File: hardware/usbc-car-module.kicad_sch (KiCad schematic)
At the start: 0 parts

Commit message: making hardware progress
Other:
- sheet FRONT USB-C POWER renamed USB-C_POWER
- added sheet ADC (ADC.kicad_sch)
- added sheet ESP-12F (ESP-12F.kicad_sch)
- note added: "ADJ BACK USB-PD BUCK-CONVERTER"
- note added: "USB VOLTAGE CHECK ADC ADS7128IRTER"
- note removed: "LM5157x"
- note removed: "TLE9251VSJXUMA1"
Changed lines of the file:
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@@
     (stroke (width 0) (type default))
   )
-  (polyline (pts (xy 109.22 107.95) (xy 140.97 107.95))
+  (polyline (pts (xy 109.22 107.95) (xy 153.67 107.95))
     (stroke (width 0) (type default))
   )
@@
     (stroke (width 0) (type default))
   )
-  (polyline (pts (xy 144.78 111.76) (xy 144.78 144.78))
-    (stroke (width 0) (type default))
-  )
   (polyline (pts (xy 76.2 54.61) (xy 87.63 54.61))
     (stroke (width 0) (type default))
@@
   )
   (rectangle (start 134.62 44.45) (end 148.59 50.8)
-    (stroke (width 0) (type default))
-    (fill (type color) (color 134 255 169 1))
-  )
-  (rectangle (start 50.8 49.53) (end 63.5 62.23)
     (stroke (width 0) (type default))
     (fill (type color) (color 134 255 169 1))
@@
     (effects (font (size 1.27 1.27)) (justify left top))
   )
-  (text_box "ADJ BACK USB-PD\nBUCK-CONVERTER"
-    (at 82.55 119.38 0) (size 25.4 6.35)
+  (text_box "1.2V LDO"
+    (at 93.98 85.09 0) (size 11.43 3.81)
     (stroke (width 0) (type default))
     (fill (type none))
     (effects (font (size 1.27 1.27)) (justify left top))
   )
-  (text_box "1.2V LDO"
-    (at 93.98 85.09 0) (size 11.43 3.81)
+  (text_box "CAR 12V-IN"
+    (at 21.59 102.87 0) (size 13.97 6.35)
     (stroke (width 0) (type default))
     (fill (type none))
     (effects (font (size 1.27 1.27)) (justify left top))
   )
-  (text_box "CAR 12V-IN"
-    (at 21.59 102.87 0) (size 13.97 6.35)
-    (stroke (width 0) (type default))
-    (fill (type none))
-    (effects (font (size 1.27 1.27)) (justify left top))
-  )
-  (text_box "USB VOLTAGE CHECK ADC\nADS7128IRTER"
-    (at 127 146.05 0) (size 22.86 12.7)
-    (stroke (width 0) (type default))
-    (fill (type none))
-    (effects (font (size 1.27 1.27)) (justify left top))
-  )
-  (text_box "CURRENT\nSHUNT"
-    (at 142.24 105.41 0) (size 10.16 5.08)
-    (stroke (width 0) (type default))
-    (fill (type none))
-    (effects (font (size 1.27 1.27)) (justify left top))
-  )
   (text "BACK (UFP)\nUSB-C" (at 135.89 49.53 0)
     (effects (font (size 1.27 1.27)) (justify left bottom))
@@
   )
   (text "CONTROLL + ENABEL SIGNALS" (at 59.69 78.74 0)
+    (effects (font (size 1.27 1.27)) (justify left bottom))
+  )
+  (text "USB VOLTAGE CHECK \nADC\nADS7128IRTER" (at 128.27 153.67 0)
     (effects (font (size 1.27 1.27)) (justify left bottom))
   )
@@
     (effects (font (size 1.27 1.27)) (justify left bottom))
   )
+  (text "ADJ BACK USB-PD\nBUCK-CONVERTER" (at 83.82 124.46 0)
+    (effects (font (size 1.27 1.27)) (justify left bottom))
+  )
   (text "CLOCK SYNC??" (at 44.45 120.65 0)
     (effects (font (size 1.27 1.27)) (justify left bottom))
@@
     (effects (font (size 1.27 1.27)) (justify left bottom))
   )
-  (text "LM5157x" (at 90.17 129.54 0)
-    (effects (font (size 1.27 1.27)) (justify left bottom))
-  )
   (text "21V BOOST-CONVERTER" (at 44.45 105.41 0)
     (effects (font (size 1.27 1.27)) (justify left bottom))
@@
     (effects (font (size 1.27 1.27)) (justify left bottom))
   )
-  (text "TLE9251VSJXUMA1" (at 27.94 73.66 0)
-    (effects (font (size 1.27 1.27)) (justify left bottom))
-  )
   (text "ESP-12F" (at 52.07 55.88 0)
     (effects (font (size 1.27 1.27)) (justify left bottom))
@@
     (effects (font (size 1.27 1.27)) (justify left bottom))
   )
-  (sheet (at 82.55 111.76) (size 25.4 6.35) (fields_autoplaced)
-    (stroke (width 0.1524) (type solid))
-    (fill (color 0 0 0 0.0000))
-    (property "Sheetname" "FRONT USB-C POWER" (at 82.55 111.0484 0)
-      (effects (font (size 1.27 1.27)) (justify left bottom))
-    )
-    (property "Sheetfile" "FRONT USB-C POWER.kicad_sch" (at 82.55 118.6946 0)
+  (sheet (at 50.8 49.53) (size 12.7 12.7) (fields_autoplaced)
+    (stroke (width 0.1524) (type solid))
+    (fill (color 0 0 0 0.0000))
+    (property "Sheetname" "ESP-12F" (at 50.8 48.8184 0)
+      (effects (font (size 1.27 1.27)) (justify left bottom))
+    )
+    (property "Sheetfile" "ESP-12F.kicad_sch" (at 50.8 62.8146 0)
+      (effects (font (size 1.27 1.27)) (justify left top))
+    )
+    (instances
+      (project "usbc-car-module"
+        (path "/fae025e9-99c5-40c1-af6f-99dc1edbfa43" (page "6"))
+      )
+    )
+  )
+  (sheet (at 82.55 111.76) (size 25.4 13.97) (fields_autoplaced)
+    (stroke (width 0.1524) (type solid))
+    (fill (color 0 0 0 0.0000))
+    (property "Sheetname" "USB-C_POWER" (at 82.55 111.0484 0)
+      (effects (font (size 1.27 1.27)) (justify left bottom))
+    )
+    (property "Sheetfile" "FRONT USB-C POWER.kicad_sch" (at 82.55 126.3146 0)
       (effects (font (size 1.27 1.27)) (justify left top))
     )
@@
       )
     )
+  )
+  (sheet (at 127 146.05) (size 22.86 13.97) (fields_autoplaced)
+    (stroke (width 0.1524) (type solid))
+    (fill (color 0 0 0 0.0000))
+    (property "Sheetname" "ADC" (at 127 145.3384 0)
+      (effects (font (size 1.27 1.27)) (justify left bottom))
+    )
+    (property "Sheetfile" "ADC.kicad_sch" (at 127 160.6046 0)
+      (effects (font (size 1.27 1.27)) (justify left top))
+    )
+    (instances
+      (project "usbc-car-module"
+        (path "/fae025e9-99c5-40c1-af6f-99dc1edbfa43" (page "7"))
+      )
+    )

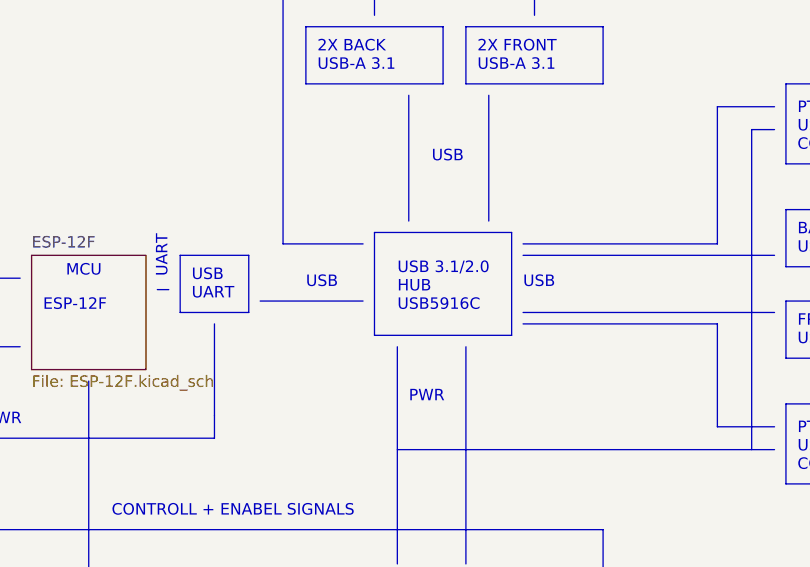
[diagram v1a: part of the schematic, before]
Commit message: working on usb side implimentaion
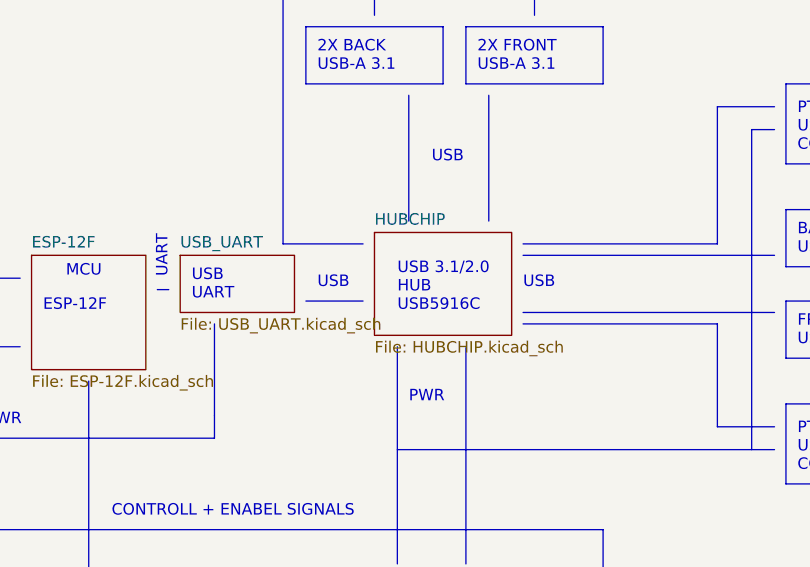
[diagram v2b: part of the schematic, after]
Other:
- added sheet HUBCHIP (HUBCHIP.kicad_sch)
- added sheet USB_UART (USB_UART.kicad_sch)
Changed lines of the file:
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@@
     (stroke (width 0) (type default))
   )
-  (polyline (pts (xy 76.2 54.61) (xy 87.63 54.61))
+  (polyline (pts (xy 81.28 54.61) (xy 87.63 54.61))
     (stroke (width 0) (type default))
   )
@@
     (stroke (width 0) (type default))
   )
-  (rectangle (start 88.9 46.99) (end 104.14 58.42)
-    (stroke (width 0) (type default))
-    (fill (type color) (color 134 255 169 1))
-  )
   (rectangle (start 134.62 54.61) (end 148.59 60.96)
     (stroke (width 0) (type default))
@@
   )
   (rectangle (start 24.13 48.26) (end 43.18 54.61)
-    (stroke (width 0) (type default))
-    (fill (type color) (color 134 255 169 1))
-  )
-  (rectangle (start 67.31 49.53) (end 74.93 55.88)
     (stroke (width 0) (type default))
     (fill (type color) (color 134 255 169 1))
@@
     (effects (font (size 1.27 1.27)) (justify left bottom))
   )
-  (text "USB" (at 81.28 53.34 0)
+  (text "USB" (at 82.55 53.34 0)
     (effects (font (size 1.27 1.27)) (justify left bottom))
   )
@@
   (text "USB" (at 95.25 39.37 0)
     (effects (font (size 1.27 1.27)) (justify left bottom))
+  )
+  (sheet (at 67.31 49.53) (size 12.7 6.35) (fields_autoplaced)
+    (stroke (width 0.1524) (type solid))
+    (fill (color 0 0 0 0.0000))
+    (property "Sheetname" "USB_UART" (at 67.31 48.8184 0)
+      (effects (font (size 1.27 1.27)) (justify left bottom))
+    )
+    (property "Sheetfile" "USB_UART.kicad_sch" (at 67.31 56.4646 0)
+      (effects (font (size 1.27 1.27)) (justify left top))
+    )
+    (property "Field2" "" (at 67.31 49.53 0)
+      (effects (font (size 1.27 1.27)) hide)
+    )
+    (instances
+      (project "usbc-car-module"
+        (path "/fae025e9-99c5-40c1-af6f-99dc1edbfa43" (page "9"))
+      )
+    )
   )
   (sheet (at 50.8 49.53) (size 12.7 12.7) (fields_autoplaced)
@@
       )
     )
+  )
+  (sheet (at 88.9 46.99) (size 15.24 11.43) (fields_autoplaced)
+    (stroke (width 0.1524) (type solid))
+    (fill (color 0 0 0 0.0000))
+    (property "Sheetname" "HUBCHIP" (at 88.9 46.2784 0)
+      (effects (font (size 1.27 1.27)) (justify left bottom))
+    )
+    (property "Sheetfile" "HUBCHIP.kicad_sch" (at 88.9 59.0046 0)
+      (effects (font (size 1.27 1.27)) (justify left top))
+    )
+    (instances
+      (project "usbc-car-module"
+        (path "/fae025e9-99c5-40c1-af6f-99dc1edbfa43" (page "8"))
+      )
+    )

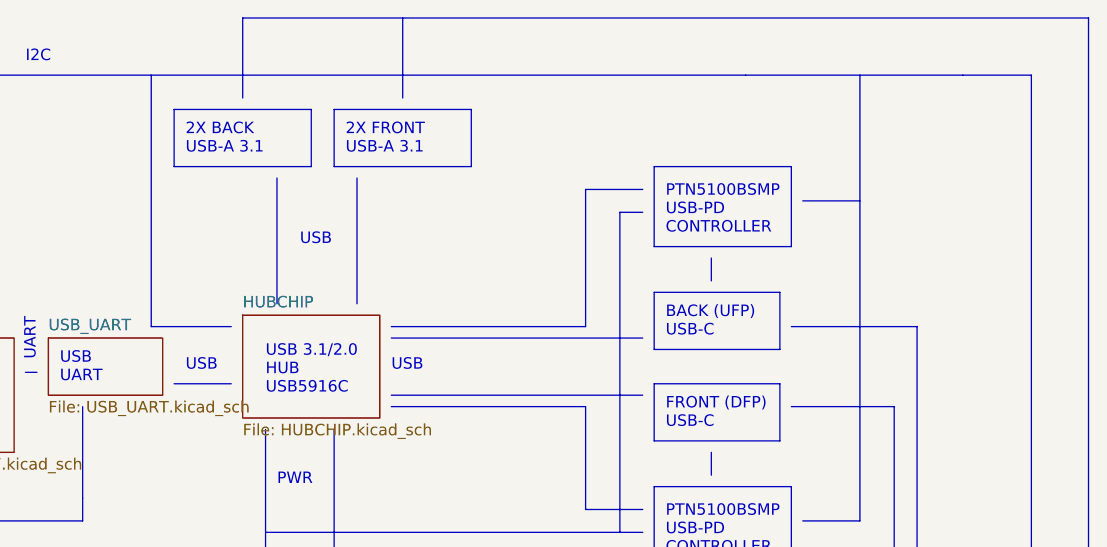
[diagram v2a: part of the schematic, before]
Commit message: working on hardware agin as well as implimentded auto adc init and read
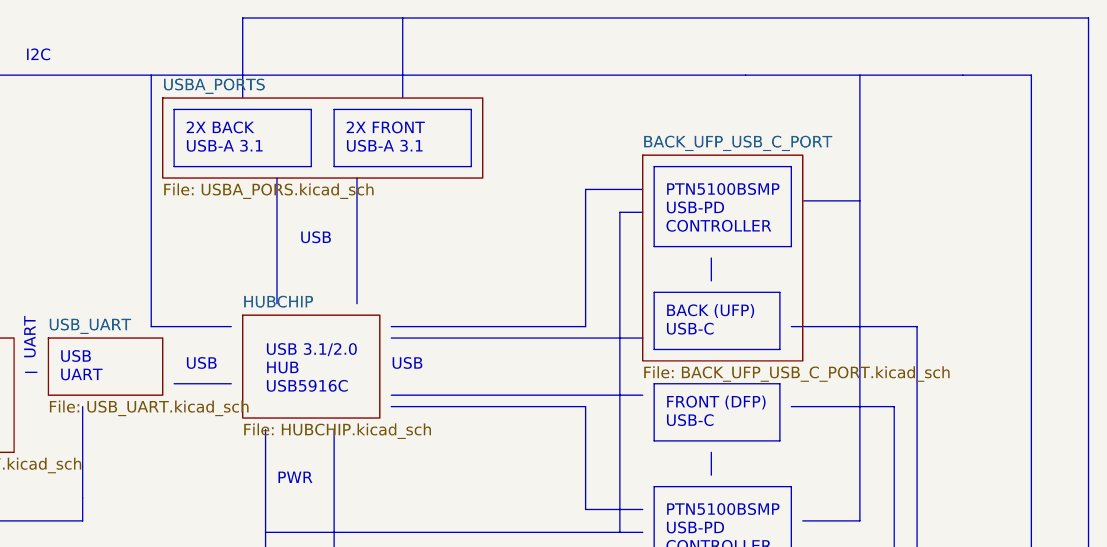
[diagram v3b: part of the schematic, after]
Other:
- added sheet BACK_UFP_USB_C_PORT (BACK_UFP_USB_C_PORT.kicad_sch)
- added sheet USBA_PORTS (USBA_PORS.kicad_sch)
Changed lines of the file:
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@@
+    )
+  )
+  (sheet (at 133.35 29.21) (size 17.78 22.86) (fields_autoplaced)
+    (stroke (width 0.1524) (type solid))
+    (fill (color 0 0 0 0.0000))
+    (property "Sheetname" "BACK_UFP_USB_C_PORT" (at 133.35 28.4984 0)
+      (effects (font (size 1.27 1.27)) (justify left bottom))
+    )
+    (property "Sheetfile" "BACK_UFP_USB_C_PORT.kicad_sch" (at 133.35 52.6546 0)
+      (effects (font (size 1.27 1.27)) (justify left top))
+    )
+    (instances
+      (project "usbc-car-module"
+        (path "/fae025e9-99c5-40c1-af6f-99dc1edbfa43" (page "11"))
+      )
     )
   )
@@
       )
     )
+  )
+  (sheet (at 80.01 22.86) (size 35.56 8.89) (fields_autoplaced)
+    (stroke (width 0.1524) (type solid))
+    (fill (color 0 0 0 0.0000))
+    (property "Sheetname" "USBA_PORTS" (at 80.01 22.1484 0)
+      (effects (font (size 1.27 1.27)) (justify left bottom))
+    )
+    (property "Sheetfile" "USBA_PORS.kicad_sch" (at 80.01 32.3346 0)
+      (effects (font (size 1.27 1.27)) (justify left top))
+    )
+    (instances
+      (project "usbc-car-module"
+        (path "/fae025e9-99c5-40c1-af6f-99dc1edbfa43" (page "10"))
+      )
+    )

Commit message: finnished rudimentry schimatics still needs alot of work
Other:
- added sheet CAR_12V_IN (CAR_12V_IN.kicad_sch)
- added sheet FRONT_DFP_USB_C_PORT (FRONT_DFP_USB_C_PORT.kicad_sch)
- added sheet FRONT_PANNEL_DISPLAY (FRONT_PANNEL_DISPLAY.kicad_sch)
- note added: "CAR 12V-IN"
- note added: "FRONT PANNEL POWER DISPLAY"
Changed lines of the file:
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@@
+    (stroke (width 0) (type default))
+  )
+  (polyline (pts (xy 39.37 31.75) (xy 46.99 31.75))
     (stroke (width 0) (type default))
   )
@@
     (stroke (width 0) (type default))
   )
+  (polyline (pts (xy 16.51 59.69) (xy 16.51 31.75))
+    (stroke (width 0) (type default))
+  )
   (polyline (pts (xy 72.39 157.48) (xy 125.73 157.48))
     (stroke (width 0) (type default))
@@
     (stroke (width 0) (type default))
   )
+  (polyline (pts (xy 16.51 31.75) (xy 19.05 31.75))
+    (stroke (width 0) (type default))
+  )
+  (polyline (pts (xy 26.67 59.69) (xy 16.51 59.69))
+    (stroke (width 0) (type default))
+  )
   (polyline (pts (xy 71.12 67.31) (xy 71.12 69.85))
     (stroke (width 0) (type default))
@@
     (stroke (width 0) (type default))
     (fill (type color) (color 134 255 169 1))
+  )
+  (rectangle (start 50.8 49.53) (end 63.5 62.23)
+    (stroke (width 0) (type default))
+    (fill (type none))
   )
   (rectangle (start 134.62 66.04) (end 149.86 74.93)
@@
     (effects (font (size 1.27 1.27)) (justify left top))
   )
-  (text_box "CAR 12V-IN"
-    (at 21.59 102.87 0) (size 13.97 6.35)
-    (stroke (width 0) (type default))
-    (fill (type none))
-    (effects (font (size 1.27 1.27)) (justify left top))
-  )
   (text "BACK (UFP)\nUSB-C" (at 135.89 49.53 0)
     (effects (font (size 1.27 1.27)) (justify left bottom))
@@
   )
   (text "IO-EXPANDER\nPI4IOE5V6416LEX" (at 25.4 53.34 0)
+    (effects (font (size 1.27 1.27)) (justify left bottom))
+  )
+  (text "CAR 12V-IN" (at 21.59 105.41 0)
     (effects (font (size 1.27 1.27)) (justify left bottom))
   )
@@
     (effects (font (size 1.27 1.27)) (justify left bottom))
   )
+  (text "FRONT PANNEL \nPOWER DISPLAY" (at 21.59 30.48 0)
+    (effects (font (size 1.27 1.27)) (justify left bottom))
+  )
   (text "ADJ BACK USB-PD\nBUCK-CONVERTER" (at 83.82 124.46 0)
     (effects (font (size 1.27 1.27)) (justify left bottom))
@@
     )
   )
-  (sheet (at 50.8 49.53) (size 12.7 12.7) (fields_autoplaced)
-    (stroke (width 0.1524) (type solid))
-    (fill (color 0 0 0 0.0000))
-    (property "Sheetname" "ESP-12F" (at 50.8 48.8184 0)
-      (effects (font (size 1.27 1.27)) (justify left bottom))
-    )
-    (property "Sheetfile" "ESP-12F.kicad_sch" (at 50.8 62.8146 0)
+  (sheet (at 21.59 46.99) (size 43.18 19.05) (fields_autoplaced)
+    (stroke (width 0.1524) (type solid))
+    (fill (color 0 0 0 0.0000))
+    (property "Sheetname" "ESP-12F" (at 21.59 46.2784 0)
+      (effects (font (size 1.27 1.27)) (justify left bottom))
+    )
+    (property "Sheetfile" "ESP-12F.kicad_sch" (at 21.59 66.6246 0)
       (effects (font (size 1.27 1.27)) (justify left top))
     )
@@
     )
   )
+  (sheet (at 20.32 102.87) (size 13.97 6.35) (fields_autoplaced)
+    (stroke (width 0.1524) (type solid))
+    (fill (color 0 0 0 0.0000))
+    (property "Sheetname" "CAR_12V_IN" (at 20.32 102.1584 0)
+      (effects (font (size 1.27 1.27)) (justify left bottom))
+    )
+    (property "Sheetfile" "CAR_12V_IN.kicad_sch" (at 20.32 109.8046 0)
+      (effects (font (size 1.27 1.27)) (justify left top))
+    )
+    (instances
+      (project "usbc-car-module"
+        (path "/fae025e9-99c5-40c1-af6f-99dc1edbfa43" (page "14"))
+      )
+    )
+  )
   (sheet (at 88.9 46.99) (size 15.24 11.43) (fields_autoplaced)
     (stroke (width 0.1524) (type solid))
@@
       )
     )
+  )
+  (sheet (at 133.35 53.34) (size 17.78 22.86) (fields_autoplaced)
+    (stroke (width 0.1524) (type solid))
+    (fill (color 0 0 0 0.0000))
+    (property "Sheetname" "FRONT_DFP_USB_C_PORT" (at 133.35 52.6284 0)
+      (effects (font (size 1.27 1.27)) (justify left bottom))
+    )
+    (property "Sheetfile" "FRONT_DFP_USB_C_PORT.kicad_sch" (at 133.35 76.7846 0)
+      (effects (font (size 1.27 1.27)) (justify left top))
+    )
+    (property "Field2" "" (at 133.35 53.34 0)
+      (effects (font (size 1.27 1.27)) hide)
+    )
+    (instances
+      (project "usbc-car-module"
+        (path "/fae025e9-99c5-40c1-af6f-99dc1edbfa43" (page "12"))
+      )
+    )
+  )
+  (sheet (at 20.32 22.86) (size 17.78 17.78) (fields_autoplaced)
+    (stroke (width 0.1524) (type solid))
+    (fill (color 0 0 0 0.0000))
+    (property "Sheetname" "FRONT_PANNEL_DISPLAY" (at 20.32 22.1484 0)
+      (effects (font (size 1.27 1.27)) (justify left bottom))
+    )
+    (property "Sheetfile" "FRONT_PANNEL_DISPLAY.kicad_sch" (at 20.32 41.2246 0)
+      (effects (font (size 1.27 1.27)) (justify left top))
+    )
+    (instances
+      (project "usbc-car-module"
+        (path "/fae025e9-99c5-40c1-af6f-99dc1edbfa43" (page "13"))
+      )
+    )

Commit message: finaliseing pcb layout will come back later for a fresh look
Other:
- company: (none) -> MICK MAKE
- title: (none) -> 200W USB PD 3.1 HUB
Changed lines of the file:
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@@
 (kicad_sch (version 20230121) (generator eeschema)
   (paper "A4")
+  (title_block
+    (title "200W USB PD 3.1 HUB")
+    (date "2023-10-03")
+    (rev "A")
+    (company "MICK MAKE")
+    (comment 1 "THIS IS A 2X 100W USB PD SOURCE ")
+    (comment 2 "HUB USB SPEC 3.1")
+    (comment 3 "TOTAL SYSTEM POWER IS ~275w")
+  )
   (polyline (pts (xy 149.86 57.15) (xy 161.29 57.15))
     (stroke (width 0) (type default))

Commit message: minor revisions
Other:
- note added: "JLC04161H-7628 CONTROLLED IMPEEDANCE"
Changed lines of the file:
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@@
     (effects (font (size 1.27 1.27)) (justify left top))
+  )
+  (text "JLC04161H-7628\nCONTROLLED IMPEEDANCE" (at 199.39 30.48 0)
+    (effects (font (size 3 3)) (justify left bottom))
   )
   (text "BACK (UFP)\nUSB-C" (at 135.89 49.53 0)
